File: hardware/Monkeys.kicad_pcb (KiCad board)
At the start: 2 copper layers, 144.9 x 59.8 mm, 142 parts, among them IC1 SI4702-C19-GM, J1 JTAG, J2 3.3vSerial, J3 Therm, J4 PJ-320D-4A, J5 10118194-0001LF, Q1 BSS138, Q2 SI2302, Q3 MMBT3904, Q4 MMBT3904, Q5 MMBT3904, Q6 MMBT3904, SW1 SW_Push, SW2 SW_Push, SW3 SW_Push, SW4 SW_Push, SW5 SPDT_Switch, SW6 SW_MEC_5E, SW7 SPDT_Switch, U1 BQ24072RGT, U2 RT9080-33GJ5, U3 CH340C, U4 LM4808, U5 InfraredReceiver, U6 ESP32-WROOM-32E(8MB), U7 Boost5V

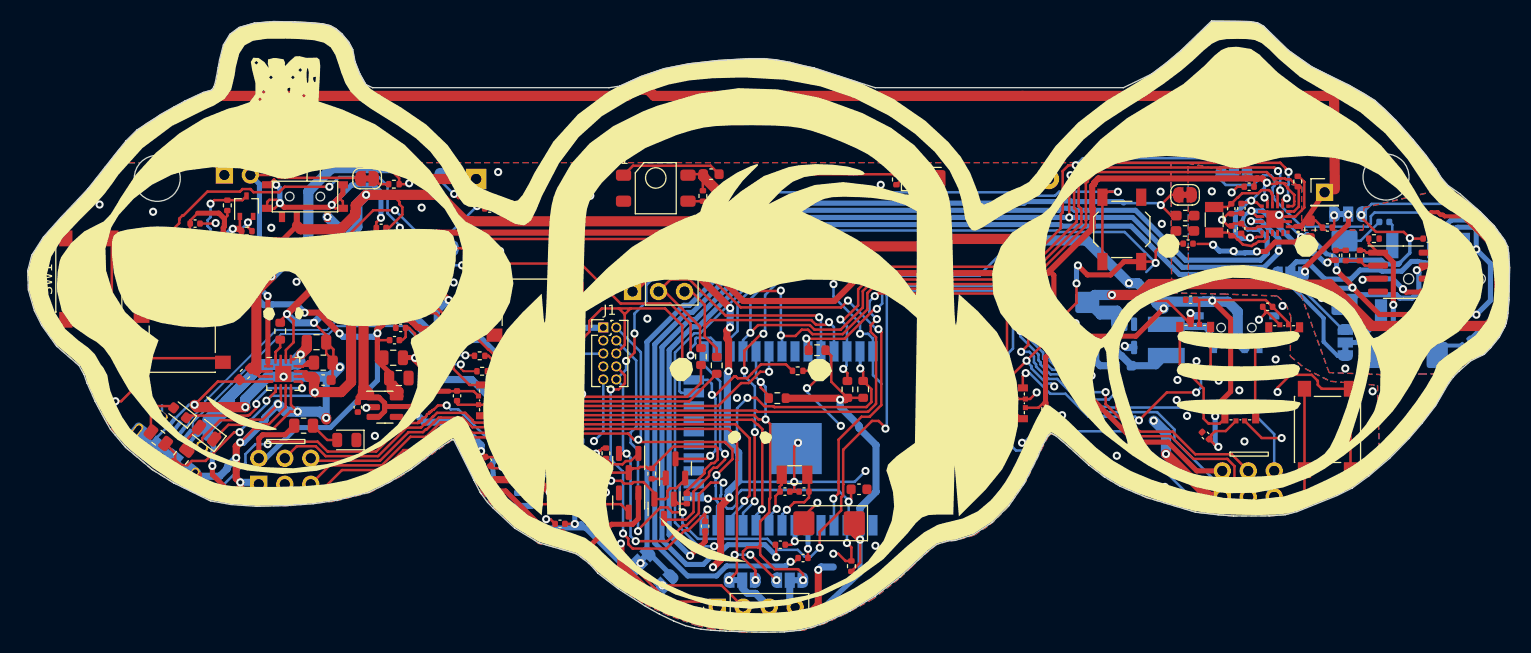
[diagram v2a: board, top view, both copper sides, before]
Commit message: hardware: Badge revision 3.5
In this revision changes were made to the following components:

- Stereo amplifier
- Microphone amplifier
- Addition of a JTAG port

This spin of the hardware went to initial manufacturing with the gerbers
provided on August 30th, 2023.
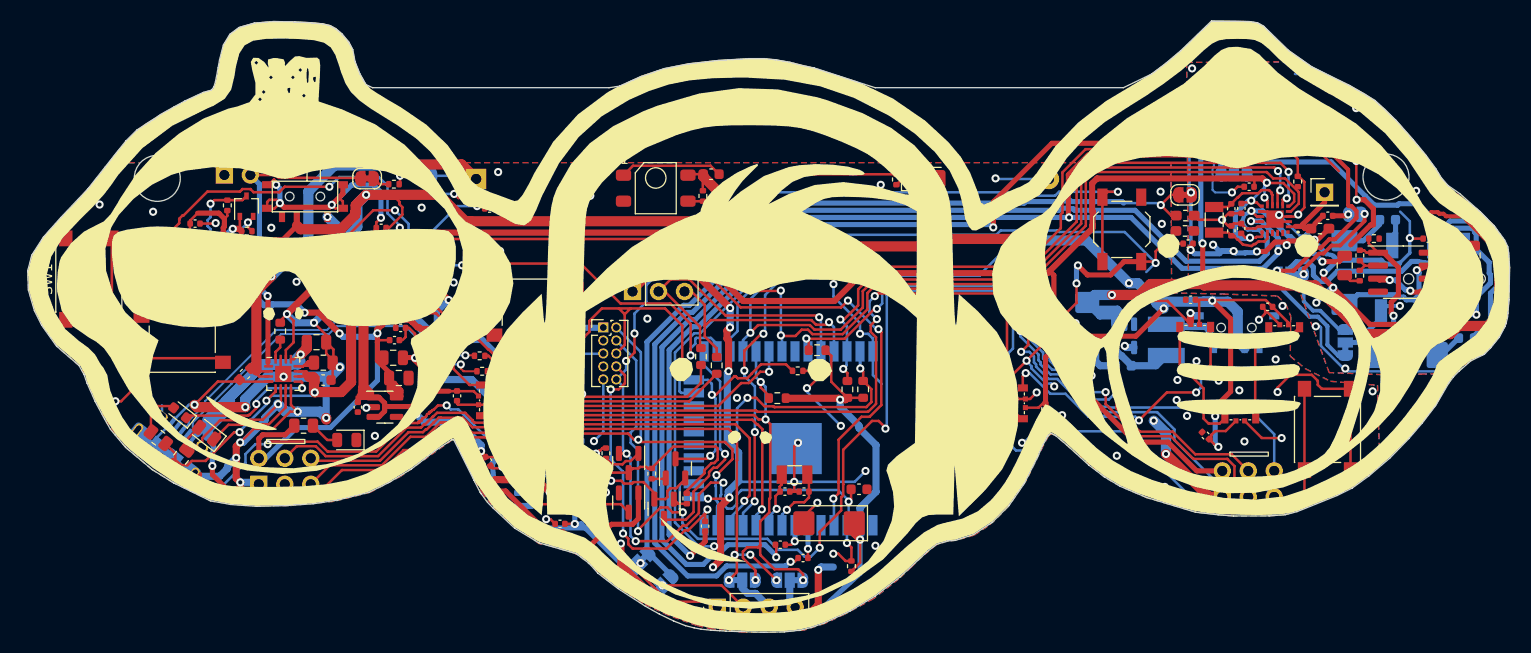
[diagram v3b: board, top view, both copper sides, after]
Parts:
- removed FB1, FB2: SCBG100505U801T, Inductor_SMD:L_0402_1005Metric
- removed the JP2 at (207.0, 68.0)
- added C42: 470nF, monkeys20221112:C_0402_1005Metric, F.Cu at (194.3, 55.1)
- added C43: 470nF, monkeys20221112:C_0402_1005Metric, F.Cu at (199.8, 58.6)
- added C44: 100nF, monkeys20221112:C_0402_1005Metric, F.Cu at (199.4, 60.5)
- added C45: 2.2uF, monkeys20221112:C_0402_1005Metric, F.Cu at (192.1, 57.7)
- added C46: 1uF, monkeys20221112:C_0402_1005Metric, F.Cu at (192.0, 59.0)
- added FB3: FB2.5K_at100mhz, Capacitor_SMD:C_0603_1608Metric, B.Cu at (218.6, 80.1)
- added FB4: FB2.5K_at100mhz, Capacitor_SMD:C_0603_1608Metric, B.Cu at (210.9, 68.5)
- added JP4: MicAmpBypass, monkeys20221112:SolderJumper-3_P1.3mm_Bridged12_RoundedPad1.0x1.5mm, B.Cu at (187.5, 60.2)
- added JP5: 0R, monkeys20221112:SolderJumper-2_P1.3mm_Bridged_RoundedPad1.0x1.5mm, B.Cu at (207.7, 68.0)
- added JP6: MicAmpPwr, Jumper:SolderJumper-2_P1.3mm_Open_RoundedPad1.0x1.5mm, B.Cu at (192.7, 61.1)
- added R38: 2.21K, monkeys20221112:R_0402_1005Metric, F.Cu at (199.7, 57.3)
- added R39: 150K, monkeys20221112:R_0402_1005Metric, F.Cu at (197.4, 55.0)
- added R40: 100K, monkeys20221112:R_0402_1005Metric, F.Cu at (199.4, 55.8)
- added U8: MAX9814, Package_DFN_QFN:DFN-14-1EP_3x3mm_P0.4mm_EP1.78x2.35mm, F.Cu at (195.8, 58.2)
- C8, C9: footprint monkeys20221112:C_0402_1005Metric -> monkeys20221112:C_0805_2012Metric
- L1: value 120Nh -> 270nH
- moved R16 2.40 mm to (208.2, 74.0), turned to 90 degrees
- moved R35 2.07 mm to (116.8, 71.4)
- moved R32 2.05 mm to (116.8, 64.2)
- moved C8 1.96 mm to (219.2, 72.0)
- moved C9 1.32 mm to (206.7, 73.0), turned to 90 degrees
- moved C15 1.14 mm to (205.1, 68.1)
- moved L1 0.98 mm to (204.3, 69.4), turned to 180 degrees
- renumbered R25 to JP2
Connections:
- net /FMIP renamed /ANT
- net /IO12 renamed /IO12_MIC
- net Net-(J4-PadR2) renamed /R2
- C32 pad 1: /MIC -> /ESP32MICin
- JP10 pad 1: /MIC -> /EARMIC
- JP9 pad 3: /MIC -> /EARMIC
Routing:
- net GNDA: track 96.2 -> 217.3 mm, vias 21 -> 35
- net /ANT: track 125.5 -> 7.61 mm
- net /MIC: track 102.4 -> 0.00 mm, vias 1 -> 0
- net /ESP32MICin: track 0.00 -> 81.9 mm, vias 0 -> 3
- net /EARMIC: track 0.00 -> 55.3 mm, vias 0 -> 2
- net /VDD: track 0.00 -> 21.3 mm, vias 0 -> 4
- net +5V: track 72.5 -> 86.8 mm, vias 1 -> 2
- net /AMPEDMIC: track 0.00 -> 6.99 mm, vias 0 -> 1
- net Net-(R39-Pad2): track 0.00 -> 3.14 mm
- net /VREF: track 12.4 -> 9.34 mm
- net Net-(JP10-Pad3): track 14.6 -> 17.6 mm
- net +3V3: track 339.3 -> 342.2 mm
- net Net-(R32-Pad2): track 3.16 -> 5.81 mm
- net Net-(C8-Pad2): track 33.4 -> 30.7 mm
- net Net-(C43-Pad1): track 0.00 -> 2.45 mm
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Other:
- board text added: "Audio Amps 5V"
- board text added: "Monkeybadge 3.5 Designed Jan 2022 - August 2023 By PacketChat, a California Small Corporation"
- board text added: "PWM/FM Lout"
- board text removed: "Headphone Amp 5V"
- board text removed: "Monkeybadge 3.4 Designed Jan 2022 - July 2023 By PacketChat, a California Small Corporation"

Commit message: hardware: Badge revision 3.6
In this revision changes were made to the following components:

- Change C42 in stereo amplifier from 390nF to 470nF
- Changed JP4 default state (Microphone amplifier - enable amplifier)

This spin of the hardware went to initial manufacturing with the gerbers
provided on September 9th, 2023.
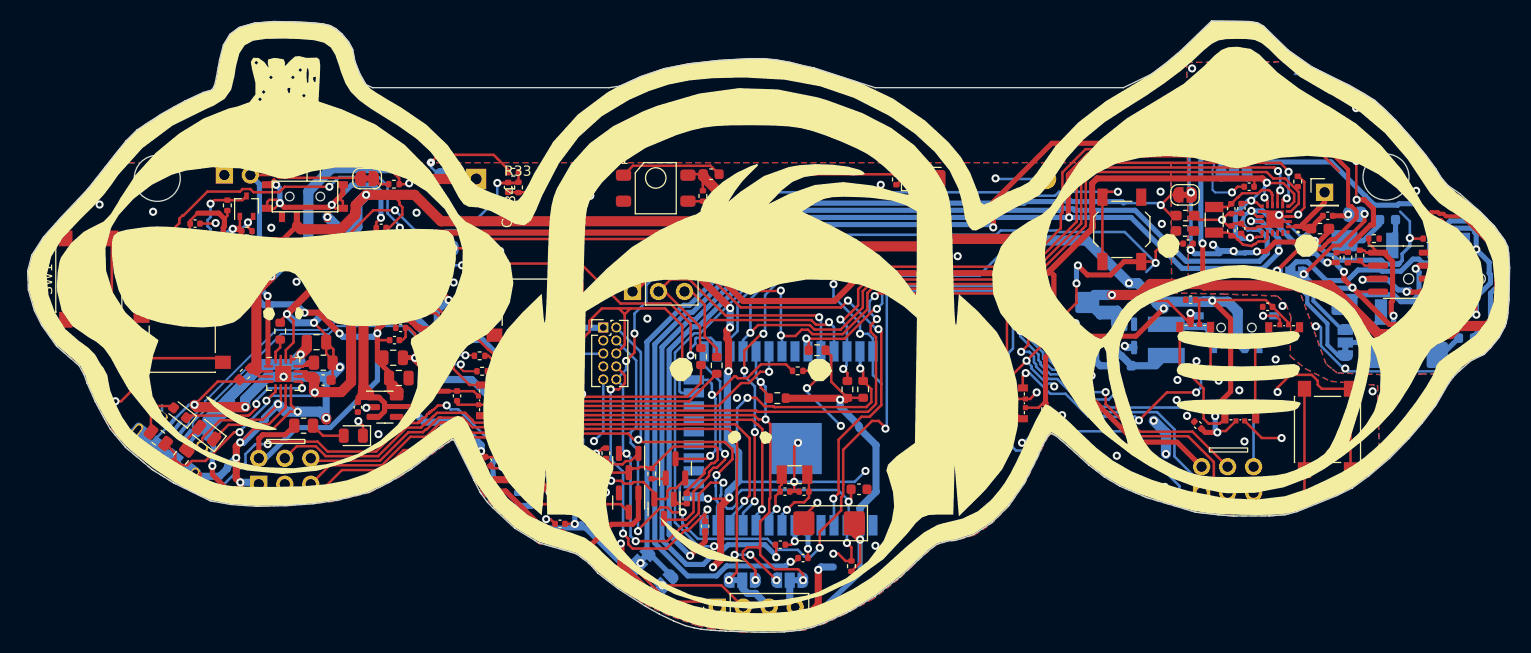
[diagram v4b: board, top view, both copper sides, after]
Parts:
- C8, C9: value 390nF -> 470nF; footprint monkeys20221112:C_0805_2012Metric -> monkeys20221112:C_0402_1005Metric
- JP6: footprint Jumper:SolderJumper-2_P1.3mm_Open_RoundedPad1.0x1.5mm -> Jumper:SolderJumper-2_P1.3mm_Bridged_RoundedPad1.0x1.5mm
- R5: value 1K -> 1.2K
- moved R33 4.94 mm to (125.4, 63.9)
- moved R34 3.01 mm to (125.9, 65.4), turned to 90 degrees
- moved C41 2.74 mm to (124.9, 65.4), turned to -90 degrees
- moved R16 2.12 mm to (207.0, 72.2), turned to -90 degrees
- moved R35 2.07 mm to (118.9, 71.3)
- moved SAO2 2.06 mm to (192.7, 92.6)
- moved R32 2.05 mm to (118.9, 64.2)
- moved C8 1.96 mm to (218.7, 73.9)
- moved C19 1.28 mm to (192.3, 88.6)
- moved C9 1.11 mm to (205.9, 72.2), turned to -90 degrees
- moved D12 0.77 mm to (109.8, 89.6)
- turned JP4 to 180 degrees
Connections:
- JP10 pad 3: Net-(JP10-Pad3) -> GNDA
- JP4 pad 1: /EARMIC -> /AMPEDMIC
- JP4 pad 3: /AMPEDMIC -> /EARMIC
- JP5 pad 1: Net-(JP10-Pad3) -> GNDA
- JP9 pad 1: Net-(JP10-Pad3) -> GNDA
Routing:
- net GNDA: track 217.3 -> 239.0 mm, vias 35 -> 37
- net Net-(JP10-Pad3): track 17.6 -> 0.00 mm, vias 2 -> 0
- net GND: track 614.1 -> 620.7 mm, vias 118 -> 122
- net +3V3: track 342.2 -> 336.9 mm
- net Net-(R32-Pad2): track 5.81 -> 10.4 mm
- net Net-(C41-Pad1): track 11.3 -> 14.9 mm
- net /VREF: track 9.34 -> 12.9 mm
- net /BATT: track 44.5 -> 42.2 mm
- net Net-(J4-PadS): track 7.37 -> 5.08 mm, vias 1 -> 0
- net /IO21_SDA1: track 98.7 -> 96.5 mm
- net /IO22_SCLK1: track 101.1 -> 98.9 mm
- net /A0: track 70.0 -> 67.9 mm
- net Net-(C8-Pad2): track 30.7 -> 32.8 mm
- net +VDC: track 235.0 -> 233.0 mm
- net /IO19_SAO2GP1: track 84.3 -> 83.1 mm
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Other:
- board text added: "Monkeybadge 3.6 Designed Jan 2022 - September 2023 By PacketChat, a California Small Corporation"
- board text removed: "Monkeybadge 3.5 Designed Jan 2022 - August 2023 By PacketChat, a California Small Corporation"

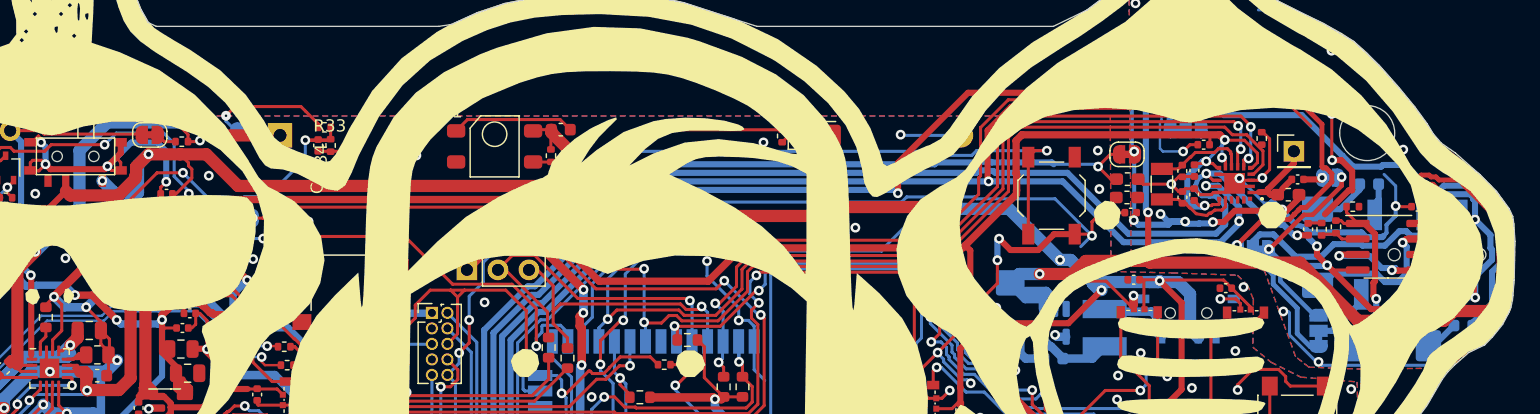
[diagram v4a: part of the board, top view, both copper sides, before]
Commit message: hardware: Badge revision 3.7
In this revision changes were made to the following components:

- Change C42 in stereo amplifier from 470nF to 390nF
- Changed JP4 default state (Microphone amplifier - disabled amp by
  default)

This spin of the hardware went to initial manufacturing with the gerbers
provided on September 15th, 2023.
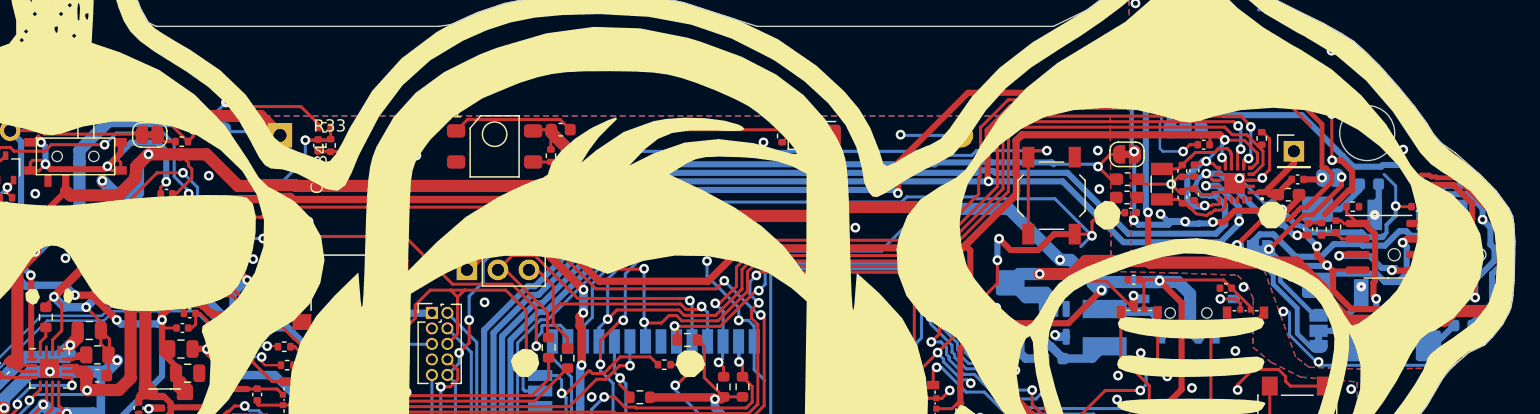
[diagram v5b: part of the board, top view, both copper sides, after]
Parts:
- C8, C9: value 470nF -> 390nF
- JP6: footprint Jumper:SolderJumper-2_P1.3mm_Bridged_RoundedPad1.0x1.5mm -> Jumper:SolderJumper-2_P1.3mm_Open_RoundedPad1.0x1.5mm
- moved R35 2.27 mm to (116.6, 71.2)
- moved R32 2.24 mm to (116.6, 64.2)
- turned JP4 to 0 degrees
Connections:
- JP4 pad 1: /AMPEDMIC -> /EARMIC
- JP4 pad 3: /EARMIC -> /AMPEDMIC
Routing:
- net +3V3: track 336.9 -> 340.3 mm
- net /BATT: track 42.2 -> 44.9 mm
- net /A0: track 67.9 -> 70.4 mm
- net Net-(C41-Pad1): track 14.9 -> 17.2 mm
- net Net-(C8-Pad2): track 32.8 -> 34.3 mm
- net GNDA: track 239.0 -> 240.3 mm
- net /T0_UP: track 80.5 -> 81.7 mm
- net Net-(R32-Pad2): track 10.4 -> 11.5 mm
- net Net-(J4-PadS): track 5.08 -> 5.72 mm, vias 0 -> 1
- net /R2: track 20.4 -> 20.3 mm, vias 0 -> 1
- net Net-(FB4-Pad1): vias 0 -> 1
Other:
- board text added: "Monkeybadge 3.7 Designed Jan 2022 - September 2023 By PacketChat, a California Small Corporation"
- board text removed: "Monkeybadge 3.6 Designed Jan 2022 - September 2023 By PacketChat, a California Small Corporation"
